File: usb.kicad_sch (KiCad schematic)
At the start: 6 parts, among them J4 USB-C

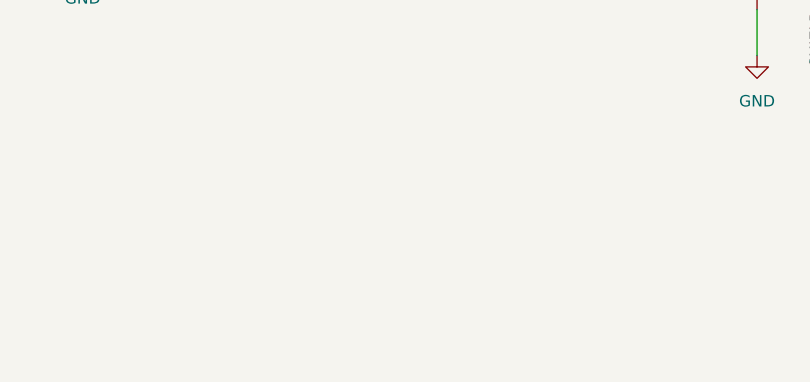
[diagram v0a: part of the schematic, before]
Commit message: relayout SDRAM
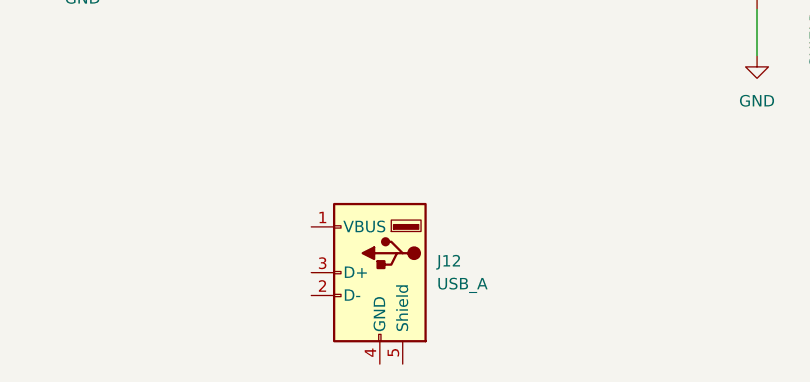
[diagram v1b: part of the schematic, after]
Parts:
- added J12: USB_A, Connector_USB:USB_A_Molex_67643_Horizontal, symbol Connector:USB_A
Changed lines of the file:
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@@
+	)
+	(symbol
+		(lib_id "Connector:USB_A")
+		(at 138.43 138.43 0)
+		(mirror y)
+		(unit 1)
+		(exclude_from_sim no)
+		(in_bom yes)
+		(on_board yes)
+		(dnp no)
+		(fields_autoplaced yes)
+		(property "Reference" "J12"
+			(at 144.78 137.1599 0)
+			(effects
+				(font
+					(size 1.27 1.27)
+				)
+				(justify right)
+			)
+		)
+		(property "Value" "USB_A"
+			(at 144.78 139.6999 0)
+			(effects
+				(font
+					(size 1.27 1.27)
+				)
+				(justify right)
+			)
+		)
+		(property "Footprint" "Connector_USB:USB_A_Molex_67643_Horizontal"
+			(at 134.62 139.7 0)
+			(effects
+				(font
+					(size 1.27 1.27)
+				)
+				(hide yes)
+			)
+		)
+		(property "Datasheet" " ~"
+			(at 134.62 139.7 0)
+			(effects
+				(font
+					(size 1.27 1.27)
+				)
+				(hide yes)
+			)
+		)
+		(property "Description" "USB Type A connector"
+			(at 138.43 138.43 0)
+			(effects
+				(font
+					(size 1.27 1.27)
+				)
+				(hide yes)
+			)
+		)
+		(pin "2"
+		)
+		(pin "4"
+		)
+		(pin "1"
+		)
+		(pin "3"
+		)
+		(pin "5"
+		)
+		(instances
+			(project "chroma-pixel-zeta"
+				(path "/70094798-b7e4-48a4-a512-b8f48be18f9f/87d5fb8c-ace9-453f-ab56-153ed16cc12a"
+					(reference "J12")
+					(unit 1)
+				)
+			)
+		)
 	)
 	(symbol

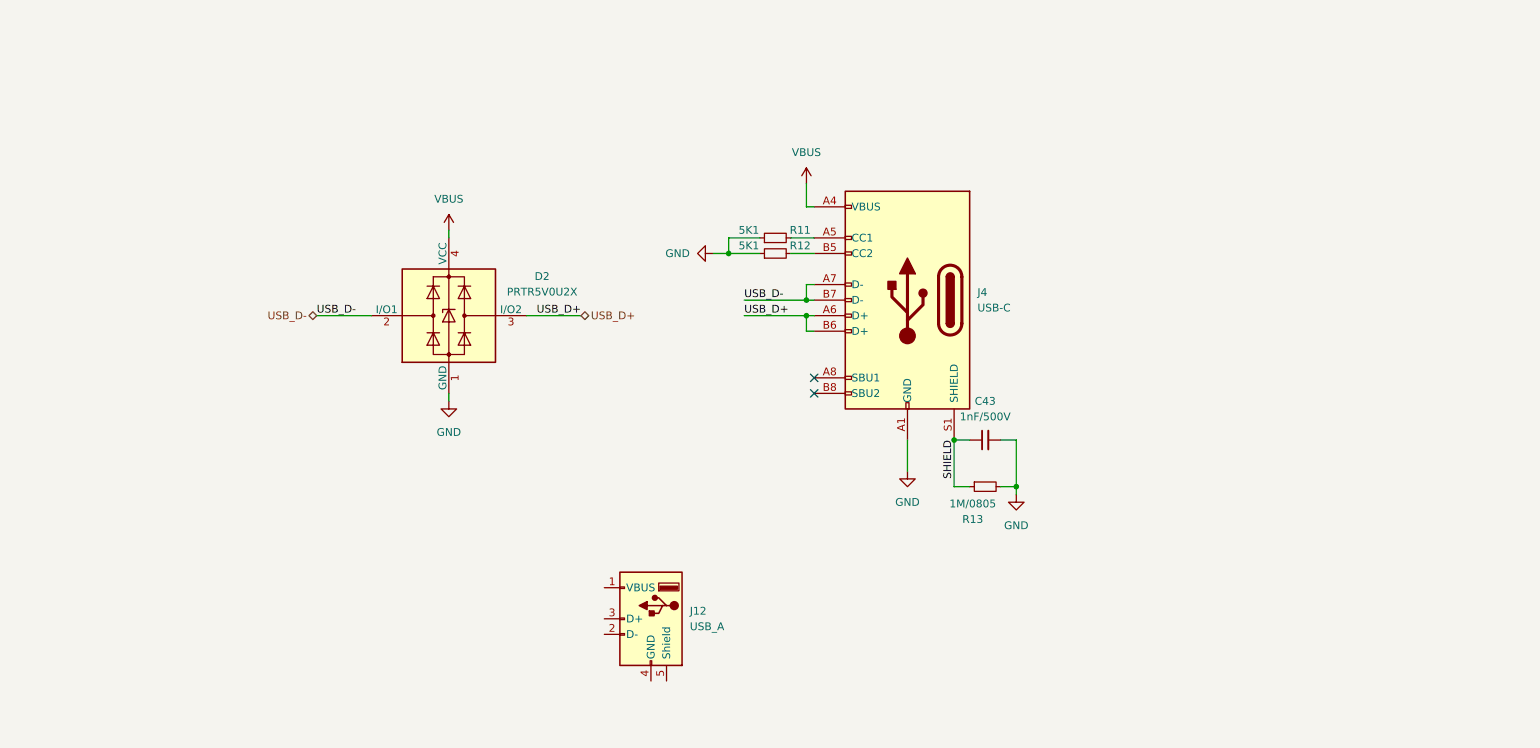
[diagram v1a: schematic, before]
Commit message: Changes: USB C to midmount, CR1220 socket, flip MCU to shorten the LCD traces
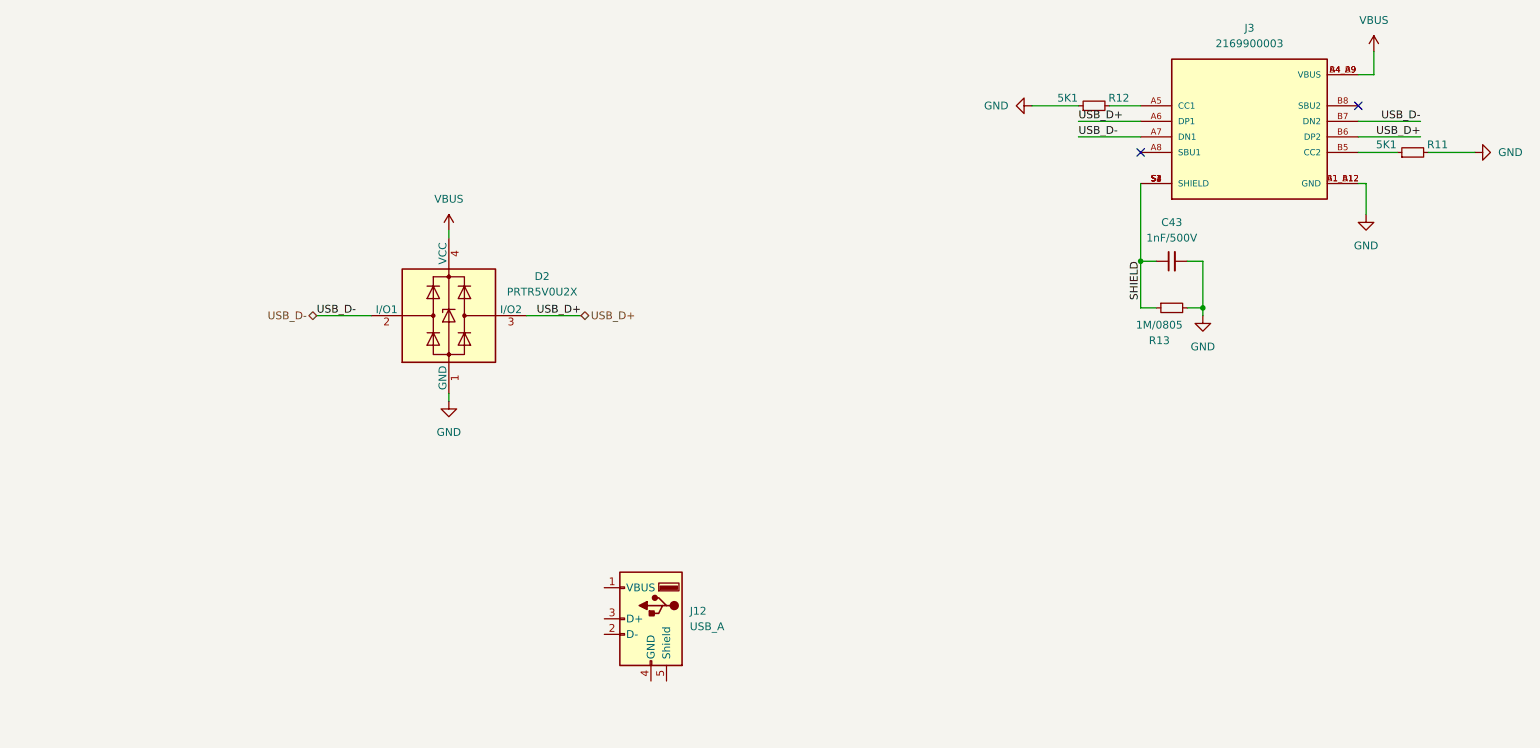
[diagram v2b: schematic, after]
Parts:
- removed J4: USB-C, Connector_USB:USB_C_Receptacle_G-Switch_GT-USB-7010ASV, symbol Connector:USB_C_Receptacle_USB2.0_16P
- added J3: 2169900003, USB_C_Mid_mount_MOLEX_2169900003:USB_C_Mid_mount_MOLEX_2169900003, symbol USB_C_Mid_mount_MOLEX_2169900003:2169900003
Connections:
- net GND: now also R11.2, J3.A1_B12 (GND), J3.B1_A12 (GND); no longer R11.1
- net SHIELD: now also J3.S1 (SHIELD), J3.S2 (SHIELD), J3.S3 (SHIELD), J3.S4 (SHIELD)
- net USB_D+: now also J3.A6 (DP1), J3.B6 (DP2)
- net USB_D-: now also J3.A7 (DN1), J3.B7 (DN2)
- net VBUS: now also J3.A4_B9 (VBUS), J3.B4_A9 (VBUS)
- net at R12.2: now also J3.A5 (CC1)
- new net: J3.B5 (CC2), R11.1
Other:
- moved on the sheet: C43, R11, R12, R13

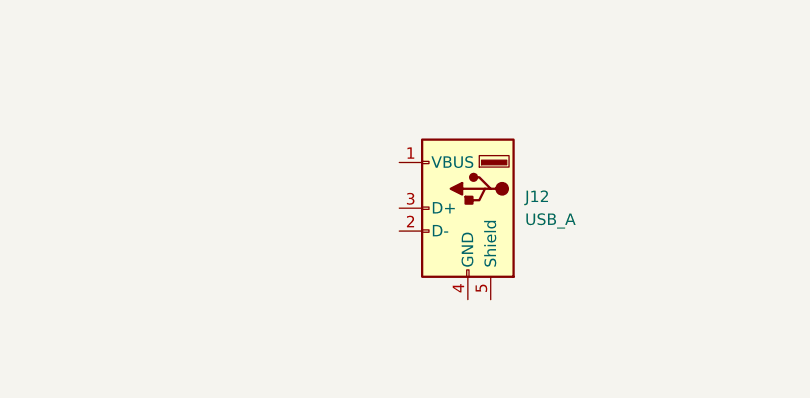
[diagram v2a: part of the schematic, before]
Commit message: Finished SDRAM, LTDC, QSPI, SDMMC, still an error on LTDC B channel
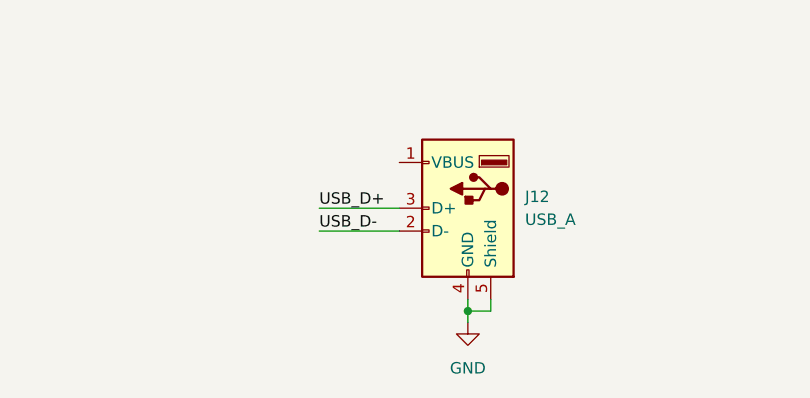
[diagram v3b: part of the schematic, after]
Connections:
- net GND: now also J12.4 (GND), J12.5 (Shield)
- net USB_D+: now also J12.3 (D+)
- net USB_D-: now also J12.2 (D-)
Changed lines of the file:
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@@
+		(color 0 0 0 0)
+	)
+	(junction
+		(at 138.43 149.86)
+		(diameter 0)
 		(color 0 0 0 0)
 	)
@@
 	(wire
 		(pts
+			(xy 138.43 148.59) (xy 138.43 149.86)
+		)
+		(stroke
+			(width 0)
+			(type default)
+		)
+	)
+	(wire
+		(pts
 			(xy 255.27 67.31) (xy 255.27 72.39)
 		)
@@
 	(wire
 		(pts
+			(xy 138.43 149.86) (xy 138.43 151.13)
+		)
+		(stroke
+			(width 0)
+			(type default)
+		)
+	)
+	(wire
+		(pts
 			(xy 127 88.9) (xy 118.11 88.9)
 		)
@@
 	(wire
 		(pts
+			(xy 140.97 149.86) (xy 138.43 149.86)
+		)
+		(stroke
+			(width 0)
+			(type default)
+		)
+	)
+	(wire
+		(pts
 			(xy 218.44 67.31) (xy 218.44 80.01)
 		)
@@
 	(wire
 		(pts
+			(xy 140.97 148.59) (xy 140.97 149.86)
+		)
+		(stroke
+			(width 0)
+			(type default)
+		)
+	)
+	(wire
+		(pts
 			(xy 220.98 87.63) (xy 218.44 87.63)
 		)
@@
 	(wire
 		(pts
+			(xy 121.92 140.97) (xy 130.81 140.97)
+		)
+		(stroke
+			(width 0)
+			(type default)
+		)
+	)
+	(wire
+		(pts
 			(xy 254 67.31) (xy 255.27 67.31)
 		)
@@
 		(pts
 			(xy 273.05 62.23) (xy 265.43 62.23)
+		)
+		(stroke
+			(width 0)
+			(type default)
+		)
+	)
+	(wire
+		(pts
+			(xy 121.92 138.43) (xy 130.81 138.43)
 		)
 		(stroke
@@
 	)
 	(label "USB_D-"
+		(at 121.92 140.97 0)
+		(fields_autoplaced yes)
+		(effects
+			(font
+				(size 1.27 1.27)
+			)
+			(justify left bottom)
+		)
+	)
+	(label "USB_D-"
 		(at 83.82 88.9 0)
 		(fields_autoplaced yes)
@@
 			)
 			(justify right bottom)
+		)
+	)
+	(label "USB_D+"
+		(at 121.92 138.43 0)
+		(fields_autoplaced yes)
+		(effects
+			(font
+				(size 1.27 1.27)
+			)
+			(justify left bottom)
 		)
 	)
@@
 					(unit 1)
 				)
+			)
+		)
+	)
+	(symbol
+		(lib_name "GND_1")
+		(lib_id "power:GND")
+		(at 138.43 151.13 0)
+		(unit 1)
+		(exclude_from_sim no)
+		(in_bom yes)
+		(on_board yes)
+		(dnp no)
+		(fields_autoplaced yes)
+		(property "Reference" "#PWR038"
+			(at 138.43 157.48 0)
+			(effects
+				(font
+					(size 1.27 1.27)
+				)
+				(hide yes)
+			)
+		)
+		(property "Value" "GND"
+			(at 138.43 156.21 0)
+			(effects
+				(font
+					(size 1.27 1.27)
+				)
+			)
+		)
+		(property "Footprint" ""
+			(at 138.43 151.13 0)
+			(effects
+				(font
+					(size 1.27 1.27)
+				)
+				(hide yes)
+			)
+		)
+		(property "Datasheet" ""
+			(at 138.43 151.13 0)
+			(effects
+				(font
+					(size 1.27 1.27)
+				)
+				(hide yes)
+			)
+		)
+		(property "Description" "Power symbol creates a global label with name \"GND\" , ground"
+			(at 138.43 151.13 0)
+			(effects
+				(font
+					(size 1.27 1.27)
+				)
+				(hide yes)
+			)
+		)
+		(pin "1"
+		)
+		(instances
+			(project "chroma-pixel-zeta"
+				(path "/70094798-b7e4-48a4-a512-b8f48be18f9f/87d5fb8c-ace9-453f-ab56-153ed16cc12a"
+					(reference "#PWR038")
+					(unit 1)
+				)

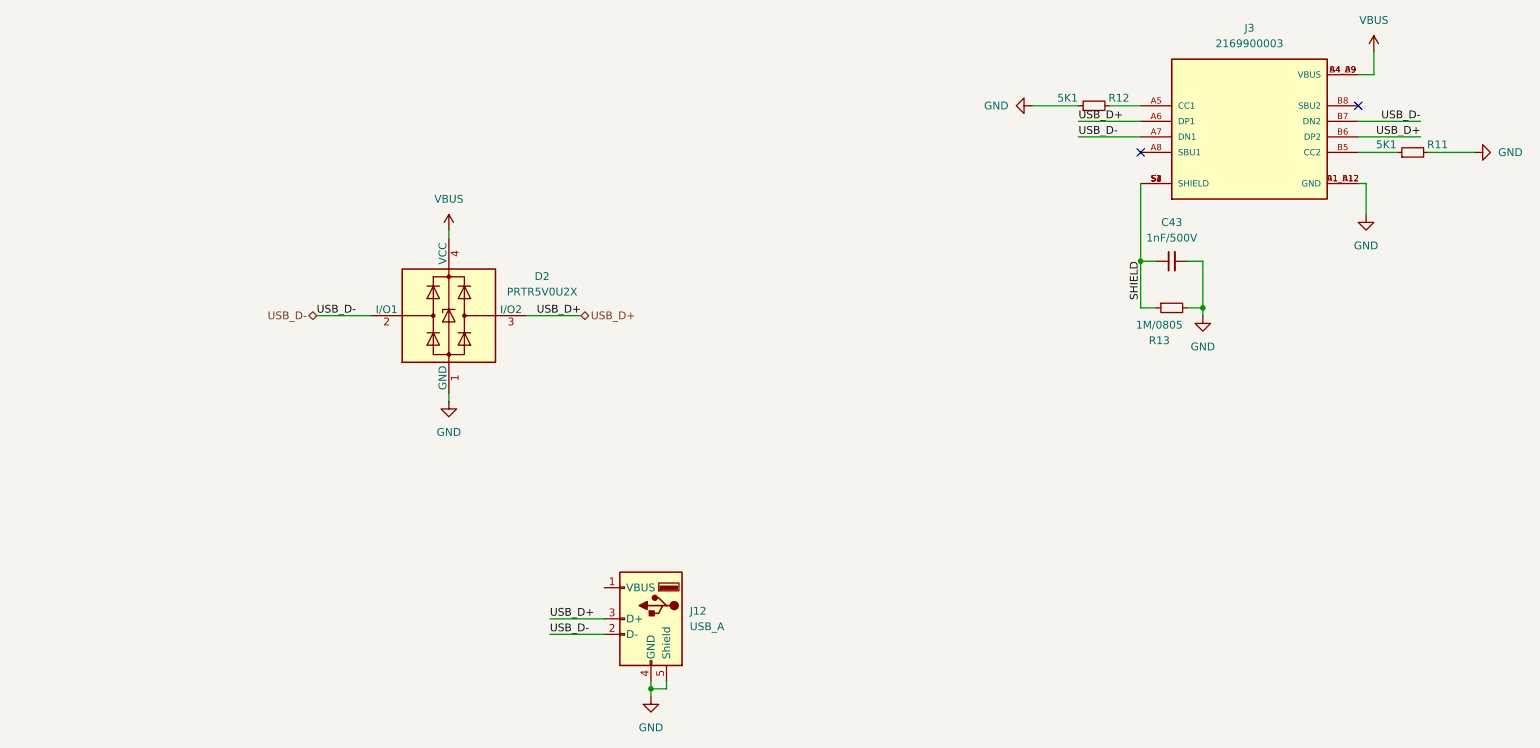
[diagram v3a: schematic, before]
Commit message: Finished SDRAM, QSPI, SDMMC, LTDC, TP, EEPROM, USB, debug (need to verify on UART)
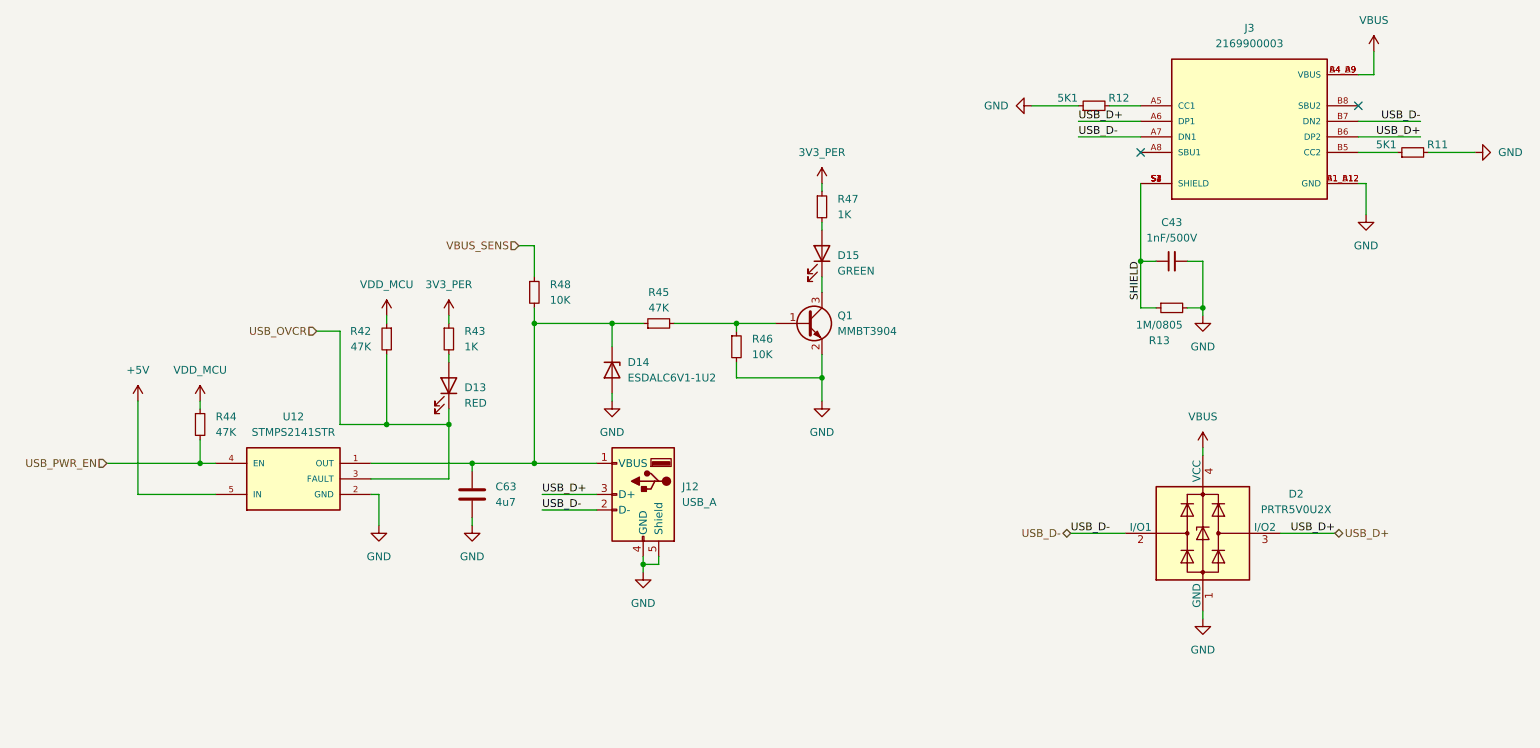
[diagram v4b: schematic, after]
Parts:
- added C63: 4u7, Capacitor_SMD:C_0805_2012Metric, symbol Device:C
- added D13: RED, LED_SMD:LED_0805_2012Metric, symbol Device:LED
- added D14: ESDALC6V1-1U2, Diode_SMD:D_SOD-523, symbol Diode:ESD5Zxx
- added D15: GREEN, LED_SMD:LED_0805_2012Metric, symbol Device:LED
- added Q1: MMBT3904, Package_TO_SOT_SMD:SOT-23, symbol Transistor_BJT:MMBT3904
- added R42, R44, R45: 47K, Resistor_SMD:R_0402_1005Metric, symbol Device:R_Small
- added R43, R47: 1K, Resistor_SMD:R_0402_1005Metric, symbol Device:R_Small
- added R46, R48: 10K, Resistor_SMD:R_0402_1005Metric, symbol Device:R_Small
- added U12: STMPS2141STR, STMPS2141STR:SOT95P280X145-5N, symbol STMPS2141STR:STMPS2141STR
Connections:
- net GND: now also C63.2, D14.2 (A), Q1.2 (E), R46.2, U12.2 (GND)
- net at J12.1 (VBUS): now also C63.1, D14.1 (K), R45.1, R48.2, U12.1 (OUT)
- new net: D15.1 (K), Q1.3 (C)
- new net: D15.2 (A), R47.2
- new net: Q1.1 (B), R45.2, R46.1
- new net: D13.2 (A), R43.2
- new net +5V: U12.5 (IN)
- new net 3V3_PER: R43.1, R47.1
- new net USB_OVCR: D13.1 (K), R42.2, U12.3 (FAULT)
- new net USB_PWR_EN: R44.2, U12.4 (EN)
- new net VBUS_SENS: R48.1
- new net VDD_MCU: R42.1, R44.1
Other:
- moved on the sheet: D2, J12

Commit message: Almost finished
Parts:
- C63: JLCPCB Part # C377773 -> C98192
- D15: JLCPCB Part # C84256 -> C2297
- J12, J3: now left out of the parts list
- Q1: JLCPCB Part # (none) -> C20526
- R43, R47: JLCPCB Part # C25741 -> C11702
- R46, R48: JLCPCB Part # C25741 -> C25744
- U12: JLCPCB Part # (none) -> C54624
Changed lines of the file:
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@@
 			)
 		)
-		(property "JLCPCB Part #" "C25741"
+		(property "JLCPCB Part #" "C25744"
 			(at 119.38 85.09 0)
 			(effects
@@
 			)
 		)
+		(property "JLCPCB Part #" "C54624"
+			(at 80.01 115.57 0)
+			(effects
+				(font
+					(size 1.27 1.27)
+				)
+				(hide yes)
+			)
+		)
 		(pin "2"
 		)
@@
 		(unit 1)
 		(exclude_from_sim no)
-		(in_bom yes)
+		(in_bom no)
 		(on_board yes)
 		(dnp no)
@@
 			)
 		)
-		(property "JLCPCB Part #" "C84256"
+		(property "JLCPCB Part #" "C2297"
 			(at 166.37 78.74 0)
 			(effects
@@
 			)
 		)
-		(property "JLCPCB Part #" "C25741"
+		(property "JLCPCB Part #" "C25744"
 			(at 152.4 93.98 0)
 			(effects
@@
 			)
 		)
-		(property "JLCPCB Part #" "C377773"
+		(property "JLCPCB Part #" "C98192"
 			(at 109.22 118.11 0)
 			(effects
@@
 			)
 		)
+		(property "JLCPCB Part #" "C20526"
+			(at 163.83 90.17 0)
+			(effects
+				(font
+					(size 1.27 1.27)
+				)
+				(hide yes)
+			)
+		)
 		(pin "2"
 		)
@@
 			)
 		)
-		(property "JLCPCB Part #" "C25741"
+		(property "JLCPCB Part #" "C11702"
 			(at 166.37 71.12 0)
 			(effects
@@
 			)
 		)
-		(property "JLCPCB Part #" "C25741"
+		(property "JLCPCB Part #" "C11702"
 			(at 105.41 92.71 0)
 			(effects
@@
 		(unit 1)
 		(exclude_from_sim no)
-		(in_bom yes)
+		(in_bom no)
 		(on_board yes)
 		(dnp no)
